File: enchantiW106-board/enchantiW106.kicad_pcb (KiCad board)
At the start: 4 copper layers, 62.2 x 25.4 mm, 65 parts, among them J1 USB_C_Receptacle_USB2.0, SW1 B3U-1000P, SW2 B3U-1000P, U1 USBLC6-2P6, U11 MAX17262REWL+T, U12 BQ25185DLHR, U13 ICM-42670-P, U2 MMC5633NJL, U3 IRIS-W106-00B, U4 NCP167AMX330TBG, U5 CP2102N-Axx-xQFN20, U6 ESP-PSRAM64, U9 NCP167AMX330TBG

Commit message: add initial software files
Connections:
- U3 pad A10: /SCL -> /TXD
- U3 pad A9: unconnected-(U3A-SDIO_D1-PadA9) -> /CTS
- U3 pad B8: unconnected-(U3A-SDIO_D0-PadB8) -> /RTS
- U3 pad B9: /SDA -> /RXD
- U3 pad L1: /RXD -> /SDA
- U3 pad L2: /TXD -> /SCL
- U3 pad L4: /RTS -> unconnected-(U3A-RMII_INT-PadL4)
- U3 pad M2: /UART_CLCK -> unconnected-(U3A-GPIO[21]-PadM2)
- U3 pad N3: /CTS -> unconnected-(U3A-GPIO[53]-PadN3)
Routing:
- net /SCL: track 39.1 -> 0.77 mm, vias 4 -> 1
- net /SDA: track 38.3 -> 0.90 mm, vias 4 -> 1
- net /RTS: track 22.8 -> 0.00 mm, vias 2 -> 0
- net /TXD: track 20.7 -> 26.5 mm, vias 0 -> 2
- net /RXD: track 20.5 -> 23.8 mm, vias 0 -> 2

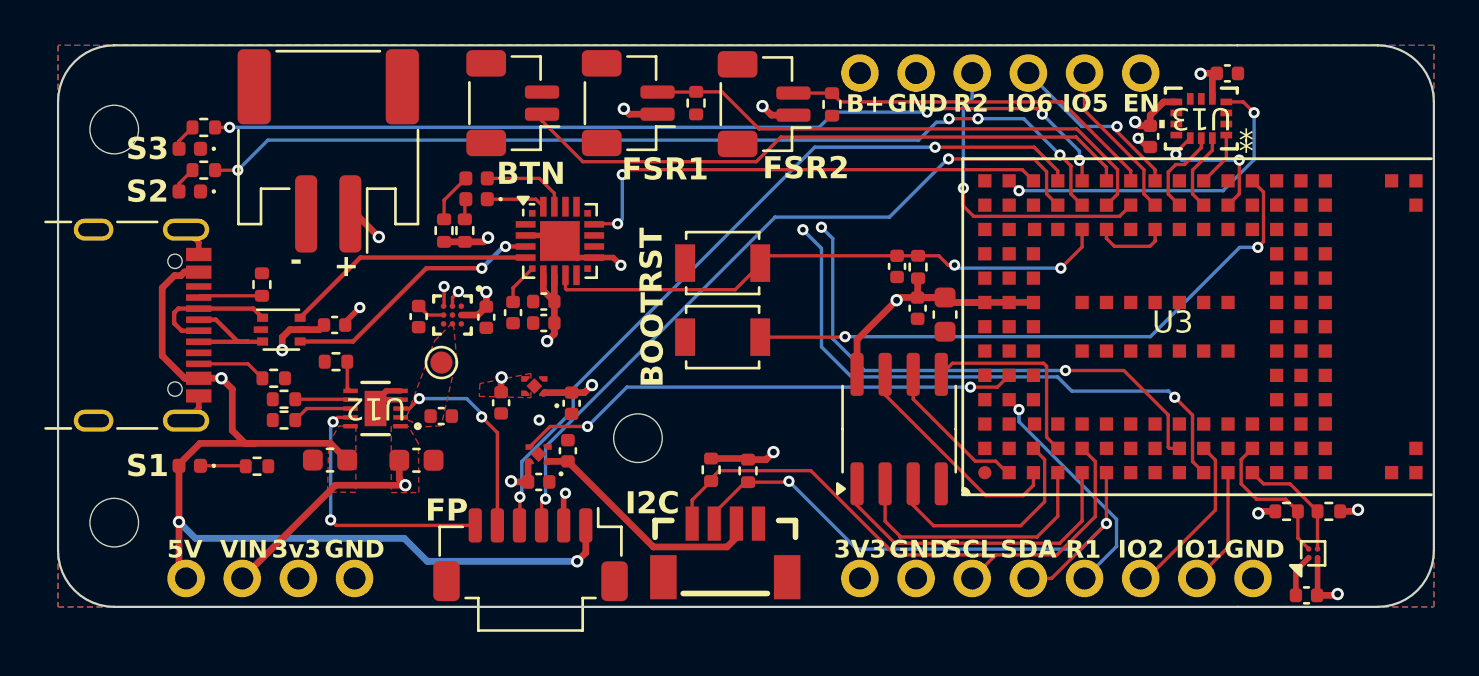
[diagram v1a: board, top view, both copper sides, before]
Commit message: fixed schematic and pcb to support in circuit programming
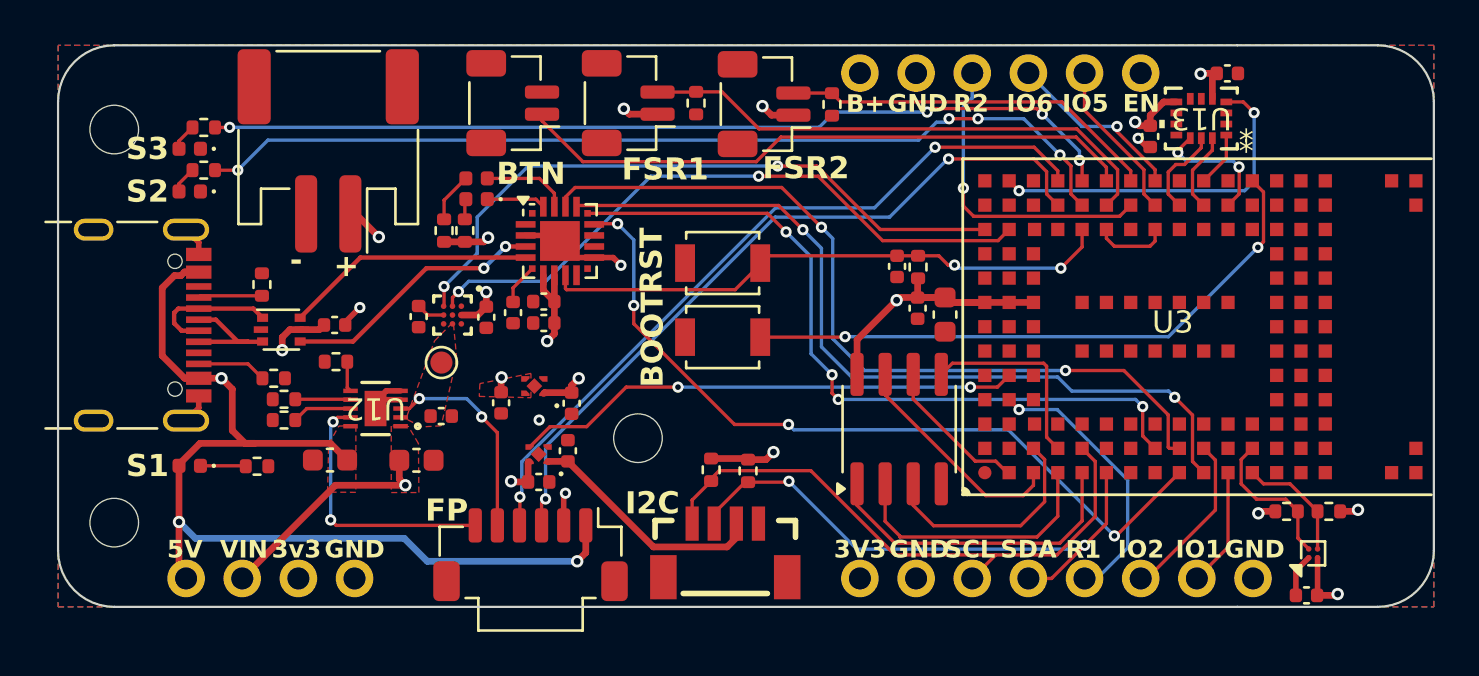
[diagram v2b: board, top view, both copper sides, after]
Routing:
- net /RTS: track 0.00 -> 33.9 mm, vias 0 -> 4
- net /SDA: track 0.90 -> 29.8 mm, vias 1 -> 2
- net /SCL: track 0.77 -> 29.3 mm, vias 1 -> 2
- net /CTS: track 22.3 -> 35.7 mm, vias 2 -> 4
- net /RXD: track 23.8 -> 36.8 mm
- net /TXD: track 26.5 -> 37.2 mm
- net /BTN_FP: track 10.7 -> 12.5 mm
- net /SDA3: track 27.4 -> 26.0 mm
- net /IMU_INT: track 15.4 -> 16.0 mm
- net /LED2: track 34.5 -> 34.0 mm

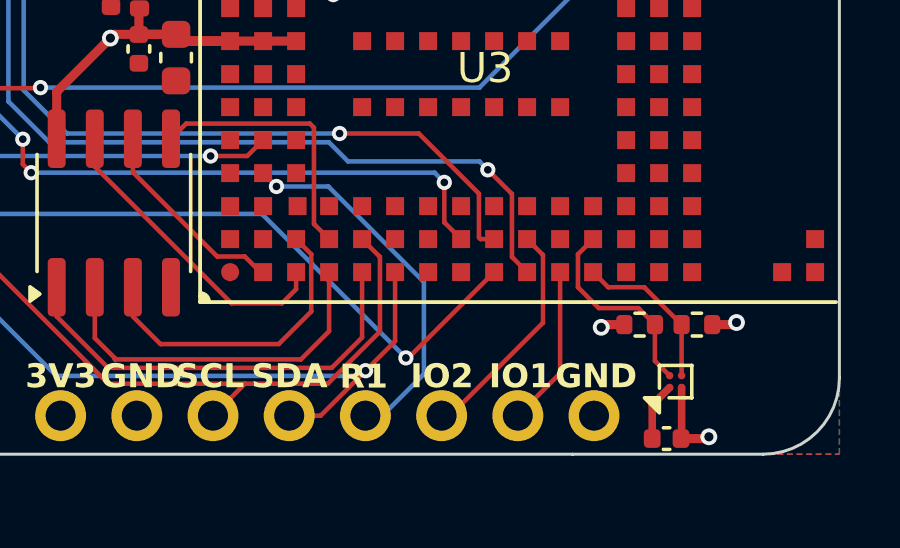
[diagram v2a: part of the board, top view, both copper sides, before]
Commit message: fixed CTS trace, updated pcbway_position and manufacturing files
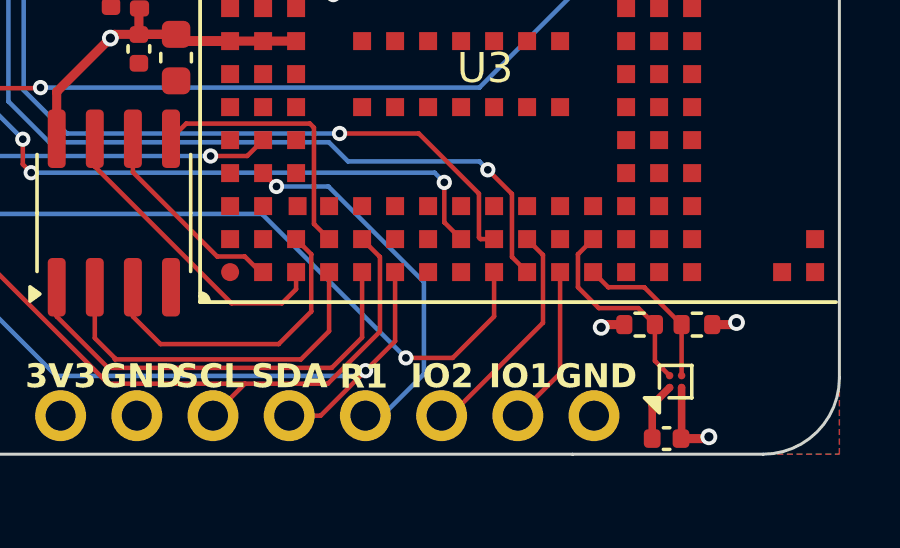
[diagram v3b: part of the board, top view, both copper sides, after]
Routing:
- net /CTS: track 35.7 -> 36.6 mm
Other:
- rule pad_to_mask_clearance: 0.0508 -> 0
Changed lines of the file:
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@@
 			(dielectric_constraints no)
 		)
-		(pad_to_mask_clearance 0.0508)
+		(pad_to_mask_clearance 0)
 		(allow_soldermask_bridges_in_footprints no)
 		(pcbplotparams
@@
 	)
 	(segment
+		(start 142.05 70.45)
+		(end 143.43 69.07)
+		(width 0.1524)
+		(layer "F.Cu")
+		(net 99)
+	)
+	(segment
 		(start 118.75 60.8504)
 		(end 118.75 60.03)
@@
 	)
 	(segment
-		(start 140.49 70.45)
-		(end 140.56999 70.45)
-		(width 0.1524)
-		(layer "F.Cu")
-		(net 99)
-	)
-	(segment
-		(start 140.56999 70.45)
+		(start 143.43 69.07)
 		(end 143.43 67.58999)
 		(width 0.1524)
@@
 		(width 0.1524)
 		(layer "F.Cu")
+		(net 99)
+	)
+	(segment
+		(start 140.49 70.45)
+		(end 142.05 70.45)
+		(width 0.1524)
+		(layer "F.Cu")

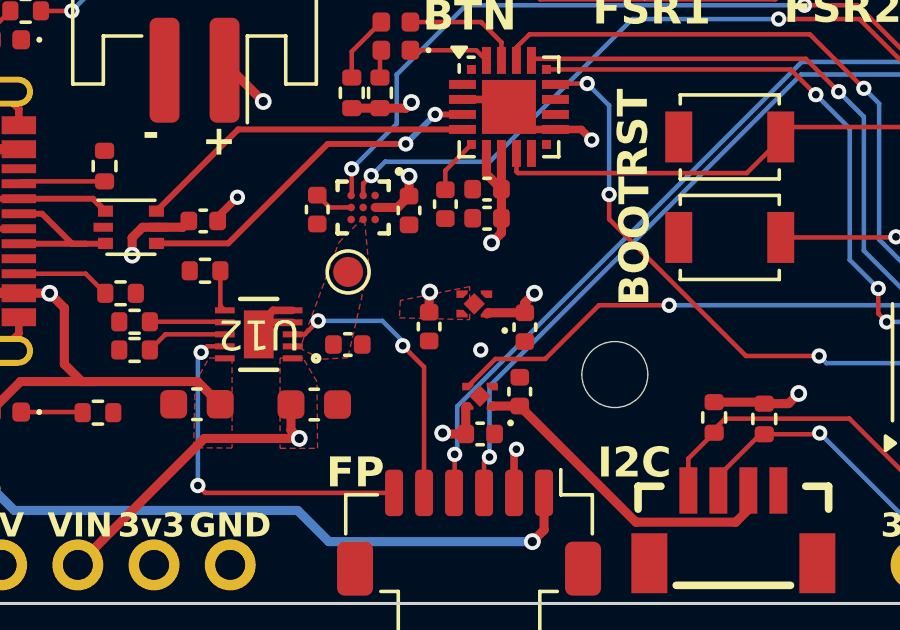
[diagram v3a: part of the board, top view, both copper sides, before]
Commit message: add git submodule for libmapper
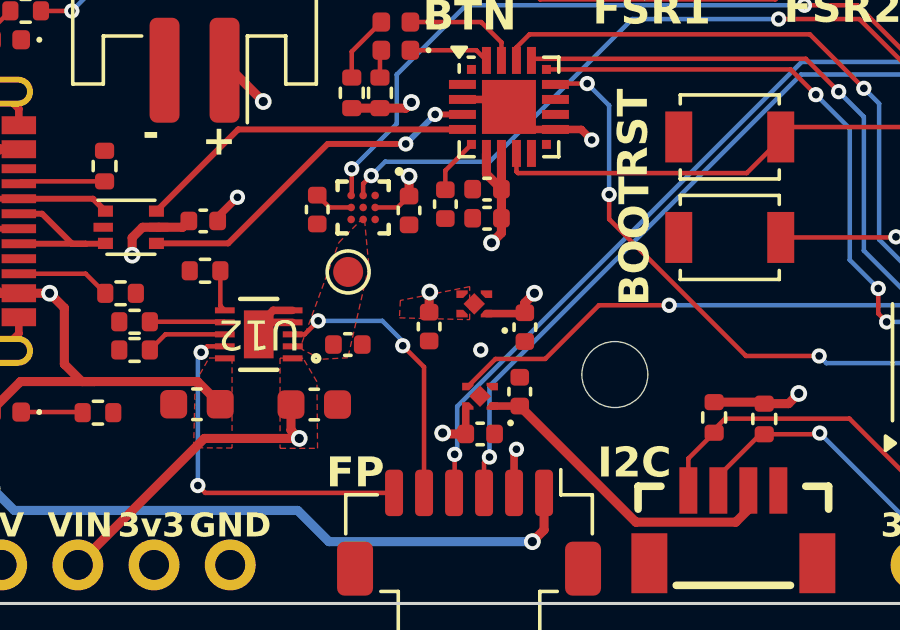
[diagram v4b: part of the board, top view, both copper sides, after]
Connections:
- U11 pad B2: GND -> unconnected-(U11-ALRT-PadB2)
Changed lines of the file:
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@@
 	(net 136 "unconnected-(U5-CLK{slash}GPIO.0-Pad2)")
 	(net 137 "unconnected-(U5-RS485{slash}GPIO.1-Pad1)")
+	(net 138 "unconnected-(U11-ALRT-PadB2)")
 	(footprint "Connector_JST:JST_PH_S2B-PH-SM4-TB_1x02-1MP_P2.00mm_Horizontal"
 		(layer "F.Cu")
@@
 			(size 0.254 0.254)
 			(layers "F.Cu" "F.Paste" "F.Mask")
-			(net 5 "GND")
+			(net 138 "unconnected-(U11-ALRT-PadB2)")
 			(pinfunction "ALRT")
-			(pintype "output")
+			(pintype "output+no_connect")
 			(clearance 0.076)
 		)
@@
 	)
 	(segment
-		(start 112.08 60.08)
-		(end 111.7 60.46)
-		(width 0.3048)
+		(start 111.7 60.46)
+		(end 112.08 60.08)
+		(width 0.1524)
 		(layer "F.Cu")
 		(net 1)
@@
 	)
 	(segment
-		(start 111.7 60.46)
-		(end 110.95 60.46)
-		(width 0.3048)
+		(start 110.95 60.46)
+		(end 111.7 60.46)
+		(width 0.1524)
 		(layer "F.Cu")
 		(net 1)
@@
 	)
 	(segment
-		(start 115.94 63.97)
-		(end 114.71462 63.97)
-		(width 0.3048)
-		(layer "F.Cu")
-		(net 4)
-	)
-	(segment
 		(start 144.922199 49.727801)
 		(end 145.12 49.53)
@@
 	)
 	(segment
-		(start 114.71462 63.97)
-		(end 114.67346 64.01116)
-		(width 0.3048)
-		(layer "F.Cu")
-		(net 4)
-	)
-	(segment
 		(start 144.922199 50.681001)
 		(end 144.922199 49.727801)
@@
 	)
 	(segment
+		(start 115.94 63.97)
+		(end 115.9123 63.9977)
+		(width 0.254)
+		(layer "F.Cu")
+		(net 4)
+	)
+	(segment
 		(start 132.83 59.665)
 		(end 130.765 59.665)
@@
 	)
 	(segment
+		(start 115.9123 63.9977)
+		(end 114.66 63.9977)
+		(width 0.254)
+		(layer "F.Cu")
+		(net 4)
+	)
+	(segment
 		(start 149.68 71.44)
 		(end 149.68 73.12)
@@
 	)
 	(segment
-		(start 113.97 67.1477)
-		(end 114.02654 67.09116)
-		(width 0.3048)
-		(layer "F.Cu")
-		(net 42)
-	)
-	(segment
 		(start 112.75 63.3)
 		(end 112.77 63.28)
@@
 	)
 	(segment
-		(start 113.97 68.01)
-		(end 113.97 67.1477)
-		(width 0.3048)
-		(layer "F.Cu")
-		(net 42)
-	)
-	(segment
 		(start 113.23 68.01)
 		(end 113.2 67.98)
@@
 		(net 42)
 	)
+	(segment
+		(start 113.97 68.01)
+		(end 113.97 67.1477)
+		(width 0.254)
+		(layer "F.Cu")
+		(net 42)
+	)
 	(via
 		(at 113.2 67.98)
@@
 	)
 	(segment
-		(start 114.87742 67.08)
-		(end 114.86626 67.09116)
-		(width 0.3048)
-		(layer "F.Cu")
-		(net 55)
-	)
-	(segment
 		(start 115.77 67.08)
 		(end 119.6404 70.9504)
@@
 	)
 	(segment
-		(start 115.77 67.08)
-		(end 114.87742 67.08)
-		(width 0.3048)
+		(start 114.8551 67.08)
+		(end 114.8528 67.0777)
+		(width 0.254)
 		(layer "F.Cu")
 		(net 55)
@@
 		(layer "F.Cu")
 		(net 55)
+	)
+	(segment
+		(start 115.77 67.08)
+		(end 114.8551 67.08)
+		(width 0.254)
+		(layer "F.Cu")
+		(net 55)

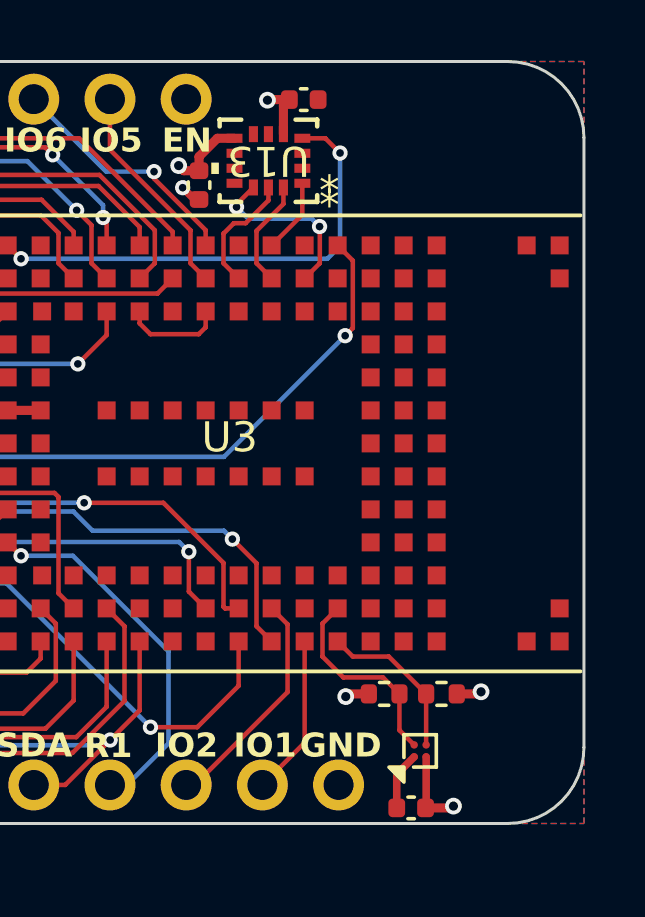
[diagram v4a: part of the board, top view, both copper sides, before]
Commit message: added axis labels to pcb silkscreen, fixed incorrect axis of magnetometer and accelerometer
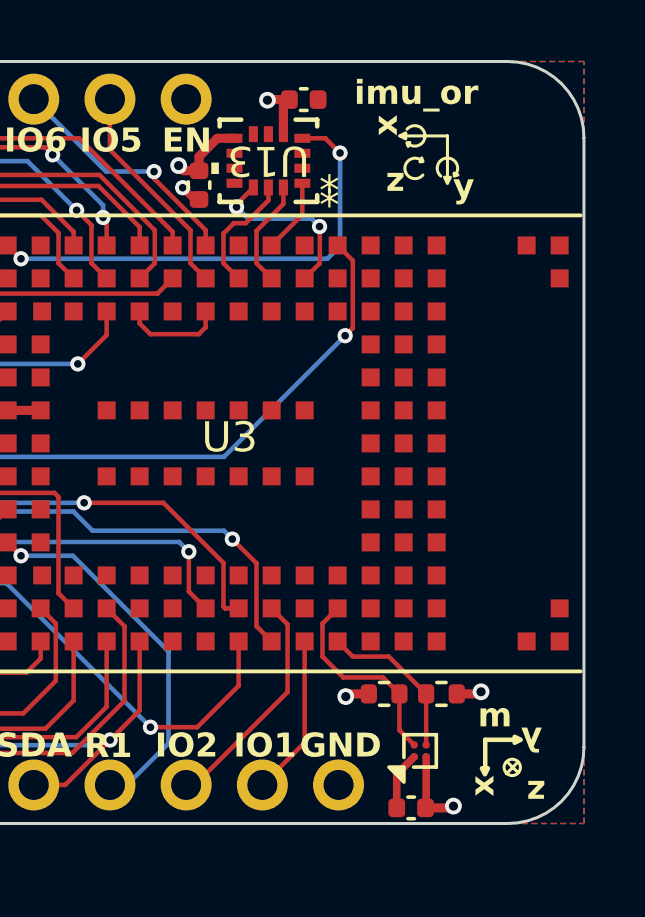
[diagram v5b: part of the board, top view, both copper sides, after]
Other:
- board text added: "T-Stick Axis"
- board text added: "X"
- board text added: "Y"
- board text added: "imu_or"
- board text removed: "a"
- board text removed: "g"
- board text removed: "n"
